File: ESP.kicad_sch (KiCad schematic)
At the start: 37 parts, among them J5 B4B-ZRLFSN, P1 B6B-ZRLFSN, P2 B6B-ZRLFSN, P3 B6B-ZRLFSN, P4 S6B-ZRLFSN, P5 B6B-ZRLFSN, P6 B6B-ZRLFSN, U3 DRV8835DSSR, U4 RP2040, U5 DRV8835DSSR, U6 DRV8835DSSR, U7 W25X40CLSS, Y1 ABM8G-12.000MHZ-4Y-T3

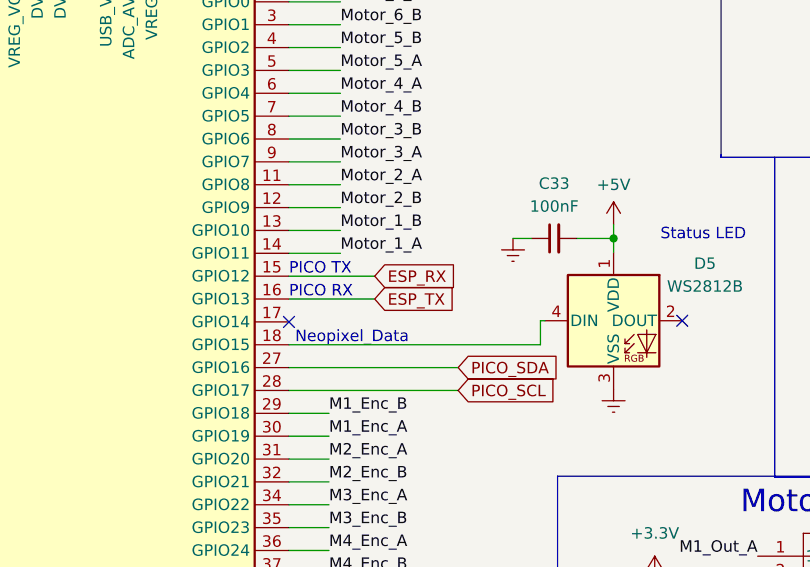
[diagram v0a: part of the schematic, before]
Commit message: update to I2C
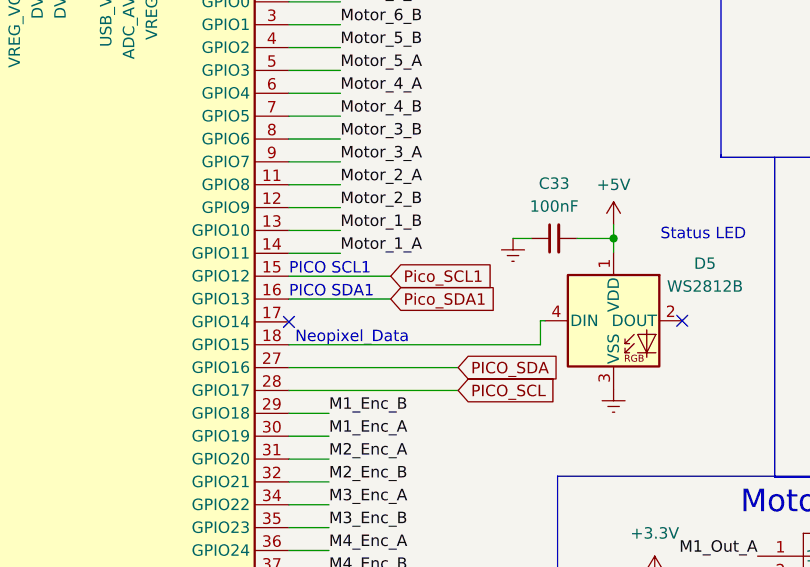
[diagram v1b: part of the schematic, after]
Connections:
- net ESP_RX renamed Pico_SCL1
- net ESP_TX renamed Pico_SDA1
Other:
- note added: "PICO SCL1"
- note added: "PICO SDA1"
- note removed: "PICO RX"
- note removed: "PICO TX"
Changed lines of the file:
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@@
     (stroke (width 0) (type default))
   )
-  (wire (pts (xy 105.664 71.628) (xy 96.139 71.628))
+  (wire (pts (xy 96.139 71.628) (xy 107.442 71.628))
     (stroke (width 0) (type default))
   )
@@
     (stroke (width 0) (type default))
   )
+  (wire (pts (xy 96.139 74.168) (xy 107.442 74.168))
+    (stroke (width 0) (type default))
+  )
   (wire (pts (xy 18.923 83.566) (xy 18.923 91.059))
     (stroke (width 0) (type default))
@@
   )
   (wire (pts (xy 100.584 114.808) (xy 96.139 114.808))
-    (stroke (width 0) (type default))
-  )
-  (wire (pts (xy 105.664 74.168) (xy 96.139 74.168))
     (stroke (width 0) (type default))
   )
@@
     (effects (font (size 2.5 2.5)) (justify left bottom))
   )
-  (text "PICO TX" (at 96.139 71.628 0)
+  (text "PICO SCL1" (at 96.139 71.628 0)
     (effects (font (size 1.27 1.27)) (justify left bottom))
   )
@@
     (effects (font (size 1.27 1.27)) (justify left bottom))
   )
-  (text "PICO RX" (at 96.139 74.168 0)
+  (text "PICO SDA1\n" (at 96.139 74.168 0)
     (effects (font (size 1.27 1.27)) (justify left bottom))
   )
@@
     (effects (font (size 1.27 1.27)) (justify left bottom))
   )
-  (global_label "ESP_RX" (shape input) (at 105.664 71.628 0) (fields_autoplaced)
+  (global_label "Pico_SCL1" (shape input) (at 107.442 71.628 0) (fields_autoplaced)
     (effects (font (size 1.27 1.27)) (justify left))
-    (property "Intersheetrefs" "${INTERSHEET_REFS}" (at 115.7248 71.628 0)
+    (property "Intersheetrefs" "${INTERSHEET_REFS}" (at 120.2243 71.628 0)
       (effects (font (size 1.27 1.27)) (justify left) hide)
     )
@@
     )
   )
-  (global_label "ESP_TX" (shape input) (at 105.664 74.168 0) (fields_autoplaced)
+  (global_label "Pico_SDA1" (shape input) (at 107.442 74.168 0) (fields_autoplaced)
     (effects (font (size 1.27 1.27)) (justify left))
-    (property "Intersheetrefs" "${INTERSHEET_REFS}" (at 115.4224 74.168 0)
+    (property "Intersheetrefs" "${INTERSHEET_REFS}" (at 120.2848 74.168 0)
       (effects (font (size 1.27 1.27)) (justify left) hide)
     )

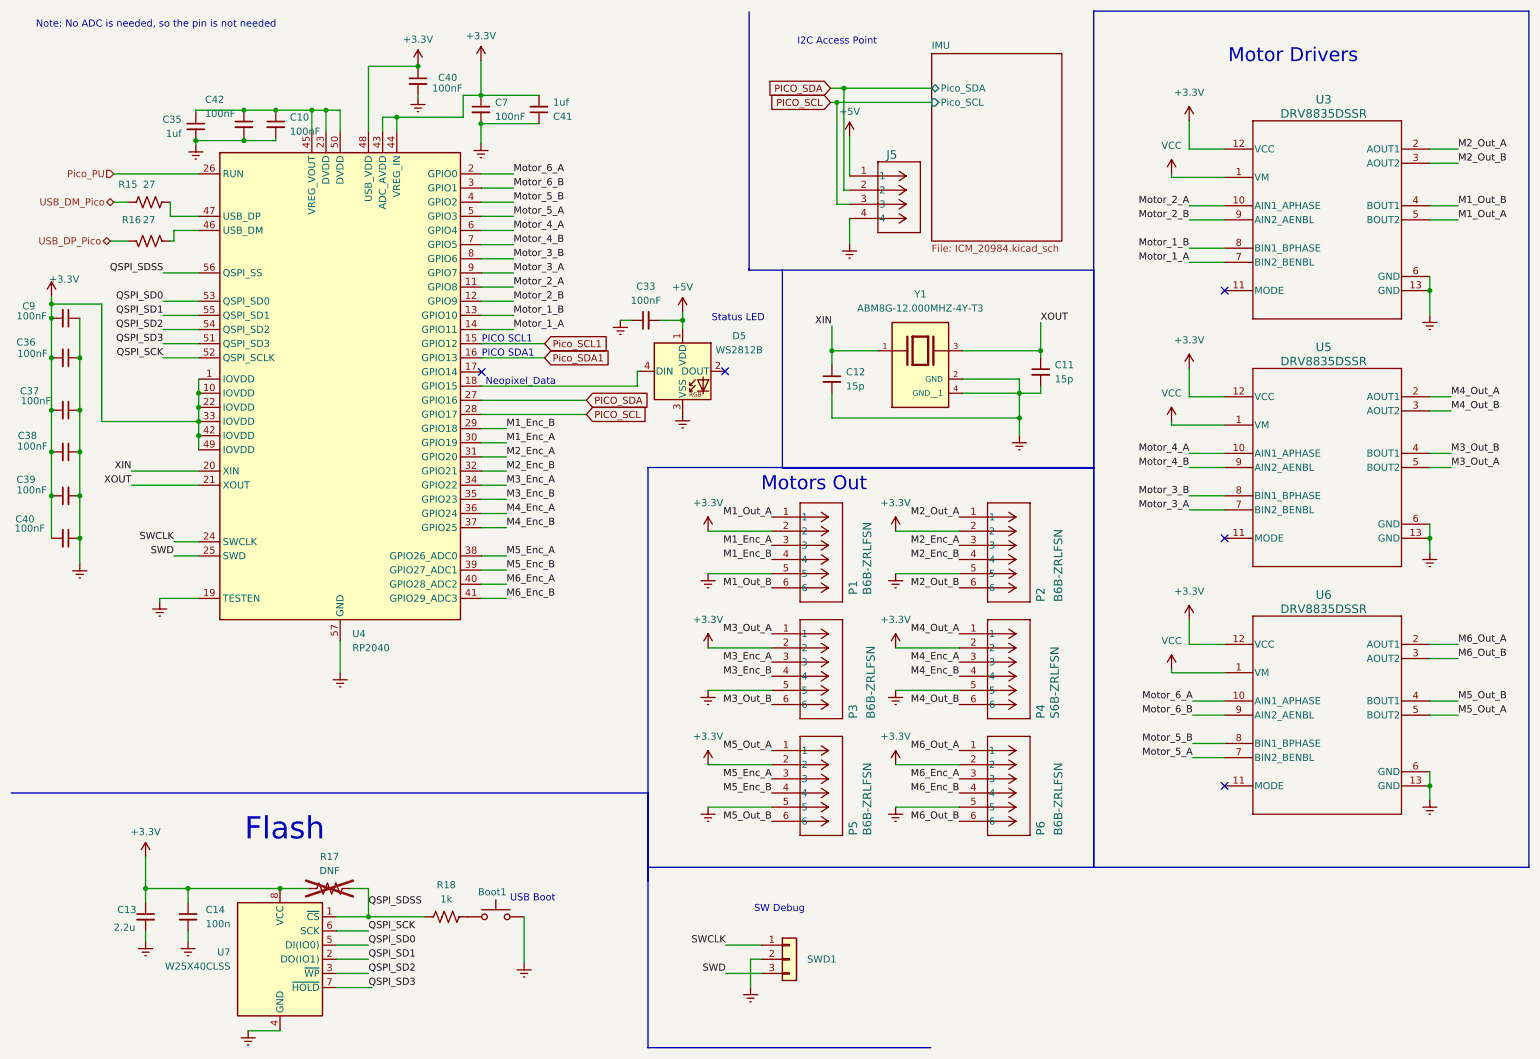
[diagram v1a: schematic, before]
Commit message: Removed 201-sized parts
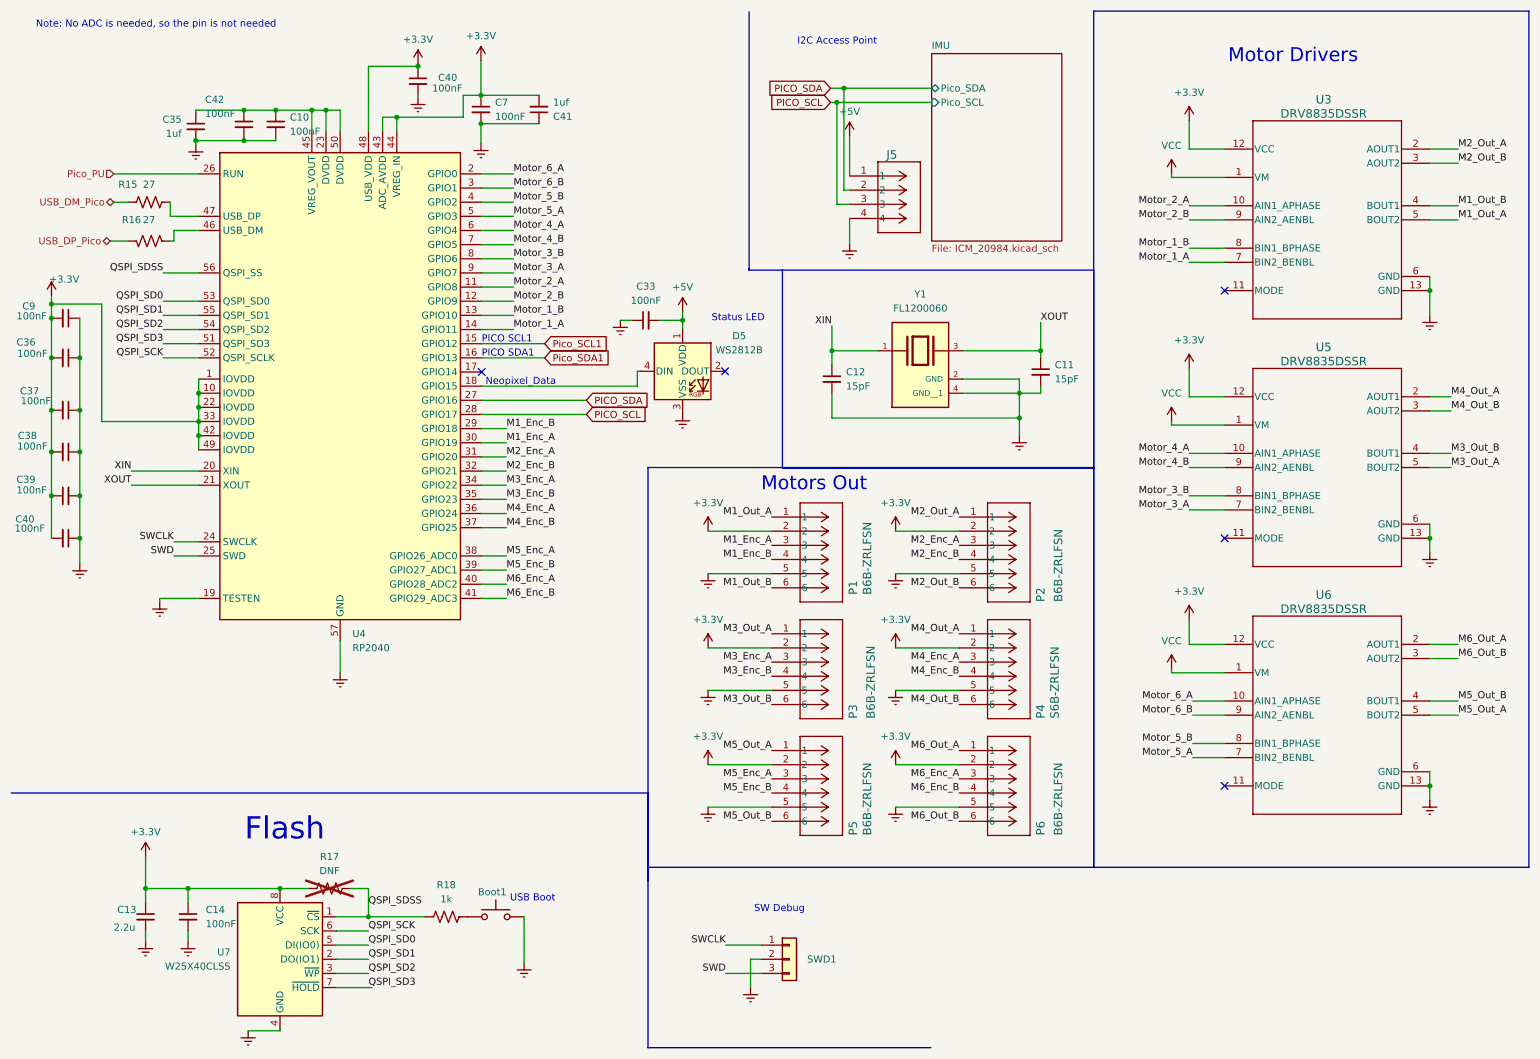
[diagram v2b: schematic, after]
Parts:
- Boot1: LCSC Part # (none) -> C116501
- C10, C36, C37, C38, C39, C40, C42, C7, C9: footprint Capacitor_SMD:C_0201_0603Metric -> Capacitor_SMD:C_0402_1005Metric; LCSC Part # (none) -> C1591
- C11, C12: value 15p -> 15pF; LCSC Part # (none) -> C86285
- C13: LCSC Part # (none) -> C12530
- C14: value 100n -> 100nF; LCSC Part # (none) -> C77020
- C33: LCSC Part # (none) -> C77020
- C35, C41: footprint Capacitor_SMD:C_0201_0603Metric -> Capacitor_SMD:C_0402_1005Metric; LCSC Part # (none) -> C14445
- C8: LCSC Part # (none) -> C1591
- D5: LCSC Part # (none) -> C114586
- R15, R16: LCSC Part # (none) -> C278580
- R18: LCSC Part # (none) -> C279987
- U3, U5, U6: LCSC Part # (none) -> C129328
- U4: LCSC Part # (none) -> C2040
- U7: LCSC Part # (none) -> C164122
- Y1: value ABM8G-12.000MHZ-4Y-T3 -> FL1200060; LCSC Part # (none) -> C1986236; MANUFACTURER Abracon -> (none); MAXIMUM_PACKAGE_HEIGHT 1.0 mm -> (none); PARTREV 08.13.15 -> (none); STANDARD Manufacturer Recommendations -> (none)

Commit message: For production
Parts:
- C10, C36, C37, C38, C39, C40, C42, C7, C9: LCSC Part # C1591 -> C1525
- C11, C12: LCSC Part # C86285 -> C1548
- C13: value 2.2u -> 2.2uF
- C14, C33: LCSC Part # C77020 -> C1525
- C35, C41: value 1uf -> 1uF; LCSC Part # C14445 -> C52923
- C8: footprint Capacitor_SMD:C_0201_0603Metric -> Capacitor_SMD:C_0402_1005Metric; LCSC Part # C1591 -> C1525
- R15, R16: value 27 -> 33; LCSC Part # C278580 -> C25105
- R18: value 1k -> 1K; LCSC Part # C279987 -> C11702
- U3, U5, U6: JLCPCB Rotation Offset (none) -> 90
- Y1: LCSC Part # C1986236 -> C5290451

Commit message: JLCniceness
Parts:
- J5: value B4B-ZRLFSN -> JST-XH; footprint JST-ZR-4Pin:CONN_B4B-ZRLFSN_JST -> Connector_JST:JST_XH_B4B-XH-AM_1x04_P2.50mm_Vertical
- U3, U5, U6: JLCPCB Rotation Offset 90 -> -90
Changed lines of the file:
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@@
 			)
 		)
-		(property "JLCPCB Rotation Offset" "90"
+		(property "JLCPCB Rotation Offset" "-90"
 			(at 248.539 138.303 0)
 			(effects
@@
 			)
 		)
-		(property "JLCPCB Rotation Offset" "90"
+		(property "JLCPCB Rotation Offset" "-90"
 			(at 248.539 49.403 0)
 			(effects
@@
 			)
 		)
-		(property "Value" "B4B-ZRLFSN"
+		(property "Value" "JST-XH"
 			(at 175.641 46.609 0)
 			(effects
@@
 			)
 		)
-		(property "Footprint" "JST-ZR-4Pin:CONN_B4B-ZRLFSN_JST"
+		(property "Footprint" "Connector_JST:JST_XH_B4B-XH-AM_1x04_P2.50mm_Vertical"
 			(at 162.179 41.529 0)
 			(effects
@@
 			)
 		)
-		(property "Datasheet" "B4B-ZRLFSN"
+		(property "Datasheet" ""
 			(at 162.179 41.529 0)
 			(effects
@@
 			)
 		)
-		(property "JLCPCB Position Offset" ""
-			(at 162.179 41.529 0)
-			(effects
-				(font
-					(size 1.27 1.27)
-				)
-				(hide yes)
-			)
-		)
 		(property "JLCPCB Rotation Offset" ""
 			(at 162.179 41.529 0)
@@
 			)
 		)
-		(property "JLCPCB Rotation Offset" "90"
+		(property "JLCPCB Rotation Offset" "-90"
 			(at 248.539 93.853 0)
 			(effects

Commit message: JLC fixes
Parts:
- J5: footprint Connector_JST:JST_XH_B4B-XH-AM_1x04_P2.50mm_Vertical -> Connector_JST:JST_XH_B4B-XH-A_1x04_P2.50mm_Vertical
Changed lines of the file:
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@@
 			)
 		)
-		(property "Footprint" "Connector_JST:JST_XH_B4B-XH-AM_1x04_P2.50mm_Vertical"
+		(property "Footprint" "Connector_JST:JST_XH_B4B-XH-A_1x04_P2.50mm_Vertical"
 			(at 162.179 41.529 0)
 			(effects
@@
 			(effects
 				(font
+					(size 1.27 1.27)
+				)
+				(hide yes)
+			)
+		)
+		(property "LCSC Part # " ""
+			(at 0 83.058 0)
+			(effects
+				(font
